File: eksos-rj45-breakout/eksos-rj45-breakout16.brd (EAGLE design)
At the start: 140 x 45 mm, 3 parts, among them X1 RJ45-8X-RC1077, X2 RJ45-8X-RC1077

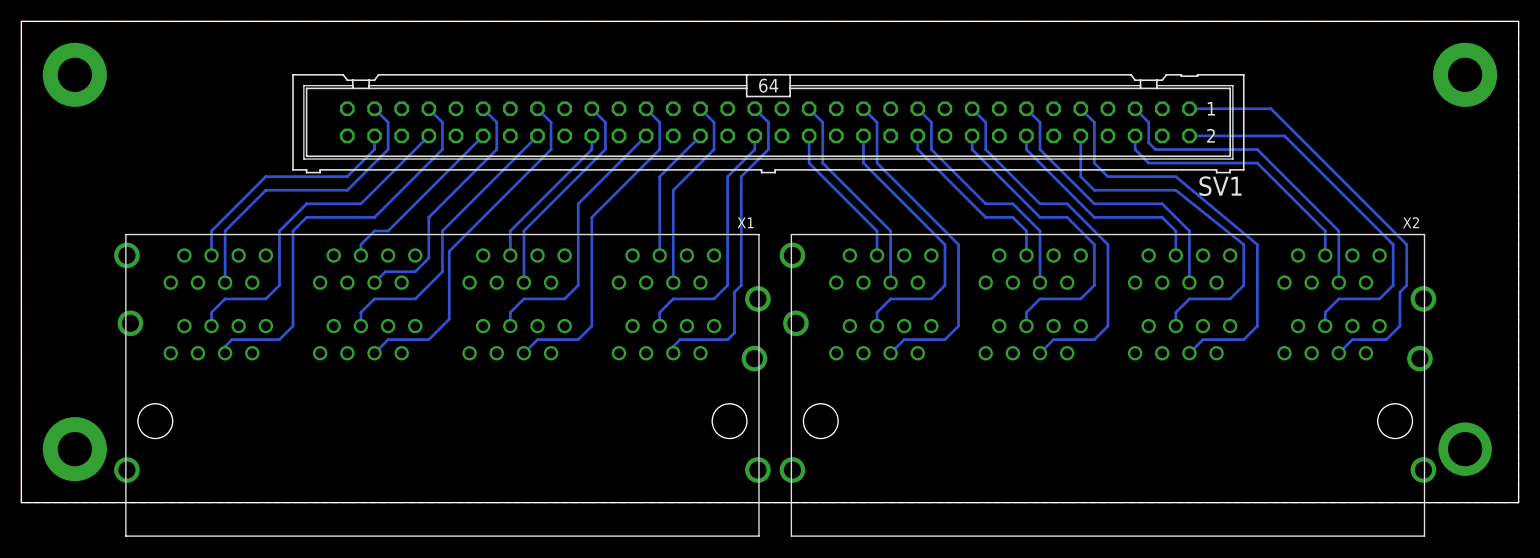
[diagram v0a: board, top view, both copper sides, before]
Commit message: eksos-rj45-breakout16: ad label/copyright/license/OSHW
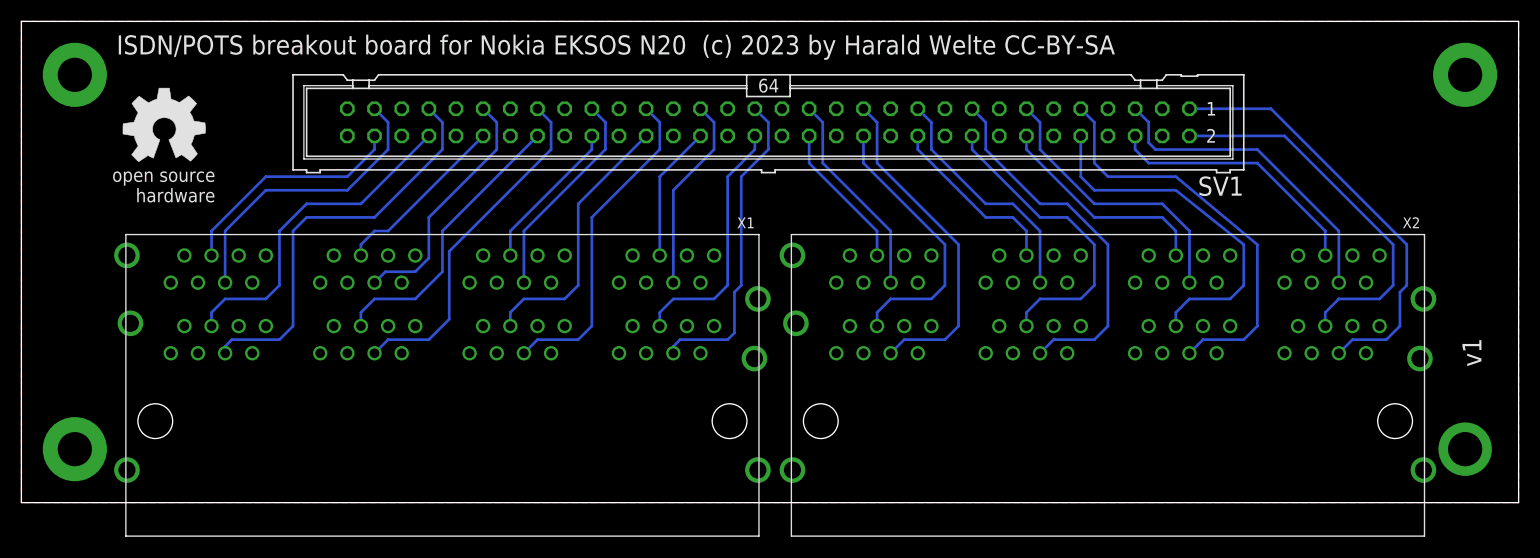
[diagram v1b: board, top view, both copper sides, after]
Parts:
- added U$1: (no value), oshw:OSHW_8MM
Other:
- board text added: ">REVISION"
- board text added: "ISDN/POTS breakout board for Nokia EKSOS N20 (c) 2023 by Harald Welte CC-BY-SA"
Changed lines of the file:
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@@
 <layer number="48" name="Document" color="7" fill="1" visible="yes" active="yes"/>
 <layer number="49" name="Reference" color="7" fill="1" visible="yes" active="yes"/>
+<layer number="50" name="dxf" color="7" fill="1" visible="no" active="no"/>
 <layer number="51" name="tDocu" color="7" fill="1" visible="yes" active="yes"/>
 <layer number="52" name="bDocu" color="7" fill="1" visible="yes" active="yes"/>
+<layer number="53" name="tGND_GNDA" color="7" fill="9" visible="no" active="no"/>
+<layer number="54" name="bGND_GNDA" color="1" fill="9" visible="no" active="no"/>
+<layer number="56" name="wert" color="7" fill="1" visible="no" active="no"/>
 <layer number="90" name="Modules" color="5" fill="1" visible="no" active="no"/>
 <layer number="91" name="Nets" color="2" fill="1" visible="no" active="no"/>
@@
 <layer number="97" name="Info" color="7" fill="1" visible="no" active="no"/>
 <layer number="98" name="Guide" color="6" fill="1" visible="no" active="no"/>
+<layer number="100" name="Muster" color="7" fill="1" visible="no" active="no"/>
+<layer number="101" name="Patch_Top" color="12" fill="4" visible="yes" active="yes"/>
+<layer number="102" name="Vscore" color="7" fill="1" visible="yes" active="yes"/>
+<layer number="103" name="tMap" color="7" fill="1" visible="yes" active="yes"/>
+<layer number="104" name="Name" color="7" fill="1" visible="yes" active="yes"/>
+<layer number="105" name="tPlate" color="7" fill="1" visible="yes" active="yes"/>
+<layer number="106" name="bPlate" color="7" fill="1" visible="yes" active="yes"/>
+<layer number="107" name="Crop" color="7" fill="1" visible="yes" active="yes"/>
+<layer number="116" name="Patch_BOT" color="9" fill="4" visible="yes" active="yes"/>
+<layer number="121" name="_tsilk" color="7" fill="1" visible="yes" active="yes"/>
+<layer number="122" name="_bsilk" color="7" fill="1" visible="yes" active="yes"/>
+<layer number="125" name="_tNames" color="7" fill="1" visible="yes" active="yes"/>
+<layer number="144" name="Drill_legend" color="7" fill="1" visible="yes" active="yes"/>
+<layer number="151" name="HeatSink" color="7" fill="1" visible="yes" active="yes"/>
+<layer number="200" name="200bmp" color="1" fill="10" visible="yes" active="yes"/>
+<layer number="201" name="201bmp" color="2" fill="1" visible="no" active="no"/>
+<layer number="202" name="202bmp" color="3" fill="1" visible="no" active="no"/>
+<layer number="203" name="203bmp" color="4" fill="10" visible="yes" active="yes"/>
+<layer number="204" name="204bmp" color="5" fill="10" visible="yes" active="yes"/>
+<layer number="205" name="205bmp" color="6" fill="10" visible="yes" active="yes"/>
+<layer number="206" name="206bmp" color="7" fill="10" visible="yes" active="yes"/>
+<layer number="207" name="207bmp" color="8" fill="10" visible="yes" active="yes"/>
+<layer number="208" name="208bmp" color="9" fill="10" visible="yes" active="yes"/>
+<layer number="209" name="209bmp" color="7" fill="1" visible="yes" active="yes"/>
+<layer number="210" name="210bmp" color="7" fill="1" visible="yes" active="yes"/>
+<layer number="211" name="211bmp" color="7" fill="1" visible="yes" active="yes"/>
+<layer number="212" name="212bmp" color="7" fill="1" visible="yes" active="yes"/>
+<layer number="213" name="213bmp" color="7" fill="1" visible="yes" active="yes"/>
+<layer number="214" name="214bmp" color="7" fill="1" visible="yes" active="yes"/>
+<layer number="215" name="215bmp" color="7" fill="1" visible="yes" active="yes"/>
+<layer number="216" name="216bmp" color="7" fill="1" visible="yes" active="yes"/>
+<layer number="250" name="Descript" color="3" fill="1" visible="no" active="no"/>
+<layer number="251" name="SMDround" color="12" fill="11" visible="no" active="no"/>
+<layer number="254" name="cooling" color="7" fill="1" visible="yes" active="yes"/>
 </layers>
 <board>
@@
 <wire x1="140" y1="45" x2="0" y2="45" width="0" layer="20"/>
 <wire x1="0" y1="45" x2="0" y2="0" width="0" layer="20"/>
+<text x="8.89" y="41.91" size="1.778" layer="25" font="vector" ratio="14">ISDN/POTS breakout board for Nokia EKSOS N20  (c) 2023 by Harald Welte CC-BY-SA</text>
+<text x="136.525" y="12.7" size="1.778" layer="25" font="vector" ratio="14" rot="R90">&gt;REVISION</text>
+<text x="131.445" y="41.91" size="1.778" layer="26" font="vector" ratio="14" rot="MR0">ISDN/POTS breakout board for Nokia EKSOS N20  (c) 2023 by Harald Welte CC-BY-SA</text>
 </plain>
 <attributes>
+<attribute name="REVISION" value="v1"/>
 </attributes>
 <variantdefs>
@@
 <element name="X1" library="stewart-rj45" package="RC01077" value="RJ45-8X-RC1077" x="39.37" y="7.62" rot="R180"/>
 <element name="X2" library="stewart-rj45" package="RC01077" value="RJ45-8X-RC1077" x="101.6" y="7.62" rot="R180"/>
+<element name="U$1" library="oshw" package="OSHW_8MM" value="" x="13.335" y="34.925"/>
 </elements>
 <signals>
@@
 </board>
 </drawing>
+<compatibility>
+<note version="6.3" minversion="6.2.2" severity="warning">
+Since Version 6.2.2 text objects can contain more than one line,
+which will not be processed correctly with this version.
+</note>
+</compatibility>
 </eagle>
